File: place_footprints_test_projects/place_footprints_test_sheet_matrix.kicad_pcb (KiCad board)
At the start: 2 copper layers, 65 parts

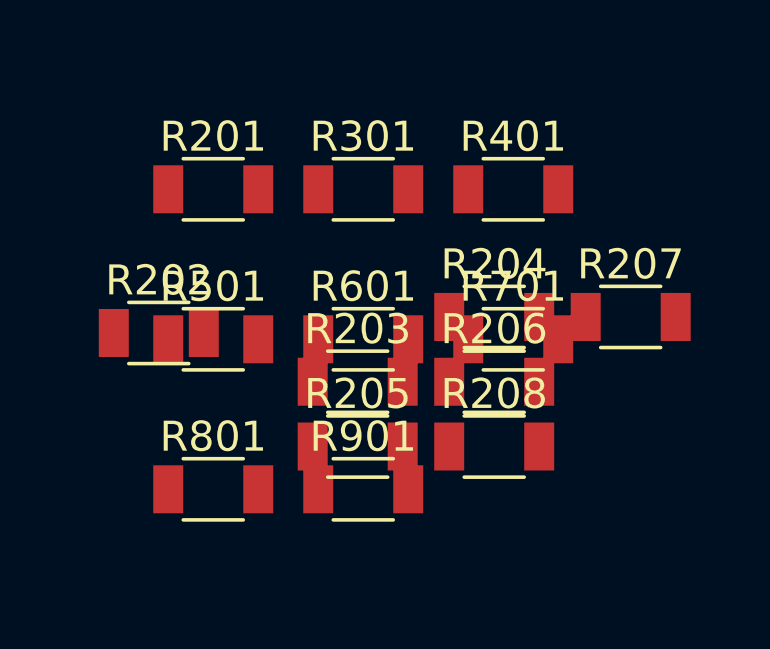
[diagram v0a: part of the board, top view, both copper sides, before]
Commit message: Update make_a_package.sh
Support footprint text placement and rotation

Add support for footprint text placement and rotation
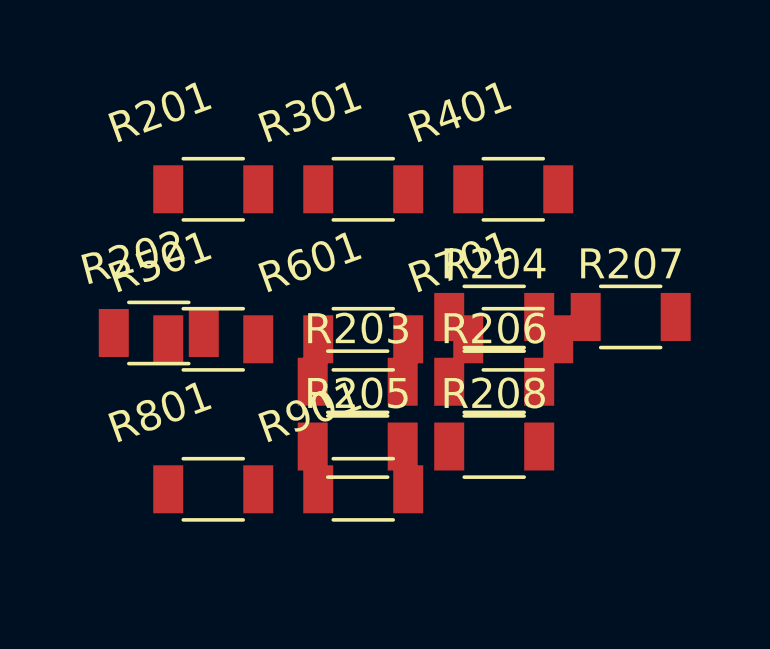
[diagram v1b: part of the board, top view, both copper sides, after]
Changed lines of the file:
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@@
     (property "Sheetname" "Sheet7")
     (attr smd)
-    (fp_text reference "R801" (at 0 -1.75) (layer "F.SilkS")
+    (fp_text reference "R801" (at -1.768 -2.568 20 unlocked) (layer "F.SilkS")
       (effects (font (size 1 1) (thickness 0.15)))
     )
@@
     (property "Sheetname" "Sheet6")
     (attr smd)
-    (fp_text reference "R701" (at 0 -1.75) (layer "F.SilkS")
+    (fp_text reference "R701" (at -1.768 -2.568 20 unlocked) (layer "F.SilkS")
       (effects (font (size 1 1) (thickness 0.15)))
     )
@@
     (property "Sheetname" "Sheet5")
     (attr smd)
-    (fp_text reference "R601" (at 0 -1.75) (layer "F.SilkS")
+    (fp_text reference "R601" (at -1.768 -2.568 20 unlocked) (layer "F.SilkS")
       (effects (font (size 1 1) (thickness 0.15)))
     )
@@
     (property "Sheetname" "Sheet8")
     (attr smd)
-    (fp_text reference "R901" (at 0 -1.75) (layer "F.SilkS")
+    (fp_text reference "R901" (at -1.768 -2.568 20 unlocked) (layer "F.SilkS")
       (effects (font (size 1 1) (thickness 0.15)))
     )
@@
     (property "Sheetname" "Sheet3")
     (attr smd)
-    (fp_text reference "R401" (at 0 -1.75) (layer "F.SilkS")
+    (fp_text reference "R401" (at -1.768 -2.568 20 unlocked) (layer "F.SilkS")
       (effects (font (size 1 1) (thickness 0.15)))
     )
@@
     (property "Sheetname" "Sheet1")
     (attr smd)
-    (fp_text reference "R202" (at 0 -1.75) (layer "F.SilkS")
+    (fp_text reference "R202" (at -0.852 -2.504 15 unlocked) (layer "F.SilkS")
       (effects (font (size 1 1) (thickness 0.15)))
     )
@@
     (property "Sheetname" "Sheet2")
     (attr smd)
-    (fp_text reference "R301" (at 0 -1.75) (layer "F.SilkS")
+    (fp_text reference "R301" (at -1.768 -2.568 20 unlocked) (layer "F.SilkS")
       (effects (font (size 1 1) (thickness 0.15)))
     )
@@
     (property "Sheetname" "Sheet1")
     (attr smd)
-    (fp_text reference "R201" (at 0 -1.75) (layer "F.SilkS")
+    (fp_text reference "R201" (at -1.768 -2.568 20 unlocked) (layer "F.SilkS")
       (effects (font (size 1 1) (thickness 0.15)))
     )
@@
     (property "Sheetname" "Sheet4")
     (attr smd)
-    (fp_text reference "R501" (at 0 -1.75) (layer "F.SilkS")
-      (effects (font (size 1 1) (thickness 0.15)))
-    )
+    (fp_text reference "R501" (at -1.768 -2.568 20 unlocked) (layer "F.SilkS")
+      (effects (font (size 1 1) (thickness 0.15)))
+    )

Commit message: update test project
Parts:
- added R101: R, Resistor_SMD:R_1210_3225Metric_Pad1.30x2.65mm_HandSolder, F.Cu at (110.5, 71.1)
- R205, R208: moved to B.Cu
- moved R403 39.9 mm to (48.8, 70.2)
- moved R405 39.9 mm to (48.8, 72.4)
- moved R406 39.9 mm to (53.3, 70.2)
- moved R407 39.9 mm to (48.8, 74.5)
- moved R402 39.9 mm to (44.2, 72.4)
- moved R404 39.9 mm to (44.2, 74.5)
- moved R408 39.9 mm to (53.3, 72.4)
- moved R205 6.25 mm to (47.0, 43.8), turned to 180 degrees
- moved R208 2.85 mm to (53.2, 40.6), turned to 180 degrees
- turned R501 to 15 degrees
- turned R601 to 15 degrees
- turned R701 to 15 degrees
- turned R801 to 30 degrees
- turned R901 to 30 degrees
